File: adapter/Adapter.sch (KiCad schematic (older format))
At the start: 13 parts, among them J1 USB_B_Micro, J2 2040210-1, J3 USB_C_Receptacle, J4 Conn_01x01, J5 Conn_01x01

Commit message: Design considerations and fixed most external circuitry for STM32
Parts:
- removed J4, J5: Conn_01x01, TestPoint:TestPoint_Keystone_5015_Micro-Minature, symbol Connector_Generic:Conn_01x01
- removed JP1, JP2: Jumper, Jumper:SolderJumper-2_P1.3mm_Bridged_RoundedPad1.0x1.5mm, symbol Device:Jumper
- removed R1: 1k, Resistor_SMD:R_0805_2012Metric, symbol Device:R
- removed R2: 2k, Resistor_SMD:R_0805_2012Metric, symbol Device:R
- added C1, C2: C_Small, symbol Device:C_Small
- added C? (x2): 20p, symbol Device:C_Small
- added C? (x5): 100n, symbol Device:C_Small
- added C?: C, symbol Device:C
- added J?: Conn_01x05_Male, symbol Connector:Conn_01x05_Male
- added L1: Ferrite_Bead_Small, symbol Device:Ferrite_Bead_Small
- added L2: CIM05U601NC, symbol Device:Ferrite_Bead_Small
- added Q?: IRLML2244TRPBF, symbol Device:Q_PMOS_GSD
- added R?: 100k, symbol Device:R
- added U1: SN75DP119, SN75DP118:QFN-20-1EP_4x4mm_P0.5mm_EP2.5x2.5mm, symbol DisplayPort_Redriver:SN75DP119
- added U2: AZ1117-3.3, symbol Regulator_Linear:AZ1117-3.3
- added U3: STM32F072C8Tx, Package_QFP:LQFP-48_7x7mm_P0.5mm, symbol MCU_ST_STM32F0:STM32F072C8Tx
- added Y?: 8MHZ, symbol Device:Crystal
- J1: symbol Connector_Specialized:USB_B_Micro -> Connector:USB_B_Micro
- J2: footprint digikey-footprints:DisplayPort_2040210-1 -> DP1RD20JQ1R400:DP1RD20JQ1R400
- J3: footprint USB_C:DX07S024WJ3R400 -> Connector_USB:USB_C_Receptacle_Amphenol_12401548E4-2A_CircularHoles; symbol Connector_Specialized:USB_C_Receptacle -> Connector:USB_C_Receptacle
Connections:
- net labels added: +3V3, DP_IN_0+, DP_IN_0-, DP_IN_1+, DP_IN_1-, DP_IN_2+, DP_IN_2-, DP_IN_3+, DP_IN_3-, DP_OUT_0+, DP_OUT_0-, DP_OUT_1+, DP_OUT_1-, EN_CTL, EQ_CTL, EXT_3.3V, PRE_CTL, SWCLK, SWDIO, VBUS_EN, VOD_CTL, nRESET
- net labels removed: D2+, D2-, DP0+, DP0-, DP1+, DP1-, DP2+, DP2-, DP3+, DP3-, pAUX+, pAUX-
- wire segments 51 -> 125
- no-connect marks 0 -> 9
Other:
- note added: "BOM\n\n8MHz Crystal -> In Stock??"
- note added: "Design Considerations.\n\nWhat to do with extra lane on DP redriver?\n -> route DP1+- as well, disable lane through EN-Z in software\n\nTerminate extra DP lanes or leave open? \n\n\nMake use of USB in STM32?-> Break out to pin headers?\n-> maybe, just maybe: connect to device USB, and leave floating?\n\n\nConnect CONFIG1/CONFIG2 to microcontroller, just in case? -> Connect CONFIG2 to CEC AF-Pin\n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"
- note added: "KiCAD Questions?\n\nEasiest way to place test points?"
- note added: "STM32 Q&A:\nDoes the VBAT need to be connected?\nDo we need special decoupling for AVDD?\nWhich are the analog pins?\n\nHow to do reset? -> can it be left floating / on SWD connector?\n\n\nWhat is BOOT0?\n\n\nHow we do programming? -> expose SWD Pins + VDD + RESET\n\nDo PF0/1 have a special function? -> Yes, the Mhz Quartz\n\nOpt to not populate Crystal? F0x2 is "crystalless USB type""
- note added: "SWD Connector\nCheck congruence with nucleo board??"
- moved on the sheet: CC1, CC2, D2+1, D2-1, J2

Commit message: cleared a bunch of questions
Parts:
- added R2, R3: <5k?, symbol Device:R
- added R4, R6: 200, symbol Device:R
- added R5, R7: 100, symbol Device:R
- added R8, R9: NF, Resistor_SMD:R_0603_1608Metric_Pad1.05x0.95mm_HandSolder, symbol Device:R
- C1, C2: value C_Small -> 100n
- C3: renamed from C?; value C -> 4u7
- J2: Digi-Key_PN A99344-ND -> (none); MPN 2040210-1 -> DP1R020JQ3
- gave numbers to parts that had none: 11
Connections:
- net CC1: now also R2.2, R4.1, R5.2
- net CC2: now also R3.2, R6.1, R7.2
- net D+: now also R9.1
- net D-: now also R8.1
- net HPD: now also U3.30 (PA9)
- net VBUS_EN: now also U3.21 (PB10)
- net at U3.32 (PA11): now also R8.2
- net at U3.33 (PA12): now also R9.2
- net at C9.1, Y1.1: no longer U3.5 (PF0)
- net at C10.1, Y1.2: no longer U3.6 (PF1)
- new net CC1_EN: R2.1
- new net CC1_RX: R4.2
- new net CC1_TX: R5.1
- new net CC2_EN: R3.1
- new net CC2_RX: R6.2
- new net CC2_TX: R7.1
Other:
- note added: "Design Considerations.\n\nWhat to do with extra lane on DP redriver?\n -> route DP1+- as well, disable lane through EN-Z in software\n-> dont route, save hassle, focus on matching DP0\n\nTerminate extra DP lanes or leave open? \n\n\nMake use of USB in STM32?-> Break out to pin headers?\n-> maybe, just maybe: connect to device USB, and leave floating?\n\n\nConnect CONFIG1/CONFIG2 to microcontrolle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"
- note added: "STM32 Q&A:\nDoes the VBAT need to be connected?\nDo we need special decoupling for AVDD?\n\nWhich are the analog pins?\nstm32f072rb.pdf p.33 ff -> PA0-PA7, PB0-\n\n5V Tolerant pins?\n-> PF0-1, PB10-11\n\n\nHow to do reset? -> can it be left floating / on SWD connector?\n\n\nWhat is BOOT0?\n\n\nHow we do programming? -> expose SWD Pins + VDD + RESET\n\nDo PF0/1 have a special function? -> Yes, the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"
- note added: "SWD Connector\nCheck congruence with nucleo board??\nSTMboards have 6 pins??"
- note removed: "BOM\n\n8MHz Crystal -> In Stock??"
- note removed: "Design Considerations.\n\nWhat to do with extra lane on DP redriver?\n -> route DP1+- as well, disable lane through EN-Z in software\n\nTerminate extra DP lanes or leave open? \n\n\nMake use of USB in STM32?-> Break out to pin headers?\n-> maybe, just maybe: connect to device USB, and leave floating?\n\n\nConnect CONFIG1/CONFIG2 to microcontroller, just in case? -> Connect CONFIG2 to CEC AF-Pin\n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"
- note removed: "STM32 Q&A:\nDoes the VBAT need to be connected?\nDo we need special decoupling for AVDD?\nWhich are the analog pins?\n\nHow to do reset? -> can it be left floating / on SWD connector?\n\n\nWhat is BOOT0?\n\n\nHow we do programming? -> expose SWD Pins + VDD + RESET\n\nDo PF0/1 have a special function? -> Yes, the Mhz Quartz\n\nOpt to not populate Crystal? F0x2 is "crystalless USB type""
- note removed: "SWD Connector\nCheck congruence with nucleo board??"
- moved on the sheet: C10, C9, Y1

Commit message: used most of stm32 pinning from twinkie board
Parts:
- added C?: 4u7, symbol Device:C_Small
- added C?: 1u, symbol Device:C_Small
- added D?: LED_ARGB, symbol Device:LED_ARGB
- added R? (x3): R, symbol Device:R
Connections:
- net labels added: LED_B_L, LED_G_L, LED_R_L, TX_CLK
- wire segments 141 -> 175
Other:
- moved on the sheet: C10, C5, C6, C7, C8, C9, L2, Y1

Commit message: pre-place most of components
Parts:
- added C13, C14, C15: 100n, Capacitor_SMD:C_0402_1005Metric, symbol Device:C_Small
- added C20: 4u7, Capacitor_SMD:C_0603_1608Metric_Pad1.05x0.95mm_HandSolder, symbol Device:C
- added R13, R14, R15: R, Resistor_SMD:R_0603_1608Metric_Pad1.05x0.95mm_HandSolder, symbol Device:R
- added SW1: SW_Push, symbol Switch:SW_Push
- C1, C10, C3, C4, C5, C6, C7, C8, C9: footprint (none) -> Capacitor_SMD:C_0603_1608Metric_Pad1.05x0.95mm_HandSolder
- C11, C12: renamed from C?; footprint (none) -> Capacitor_SMD:C_0603_1608Metric_Pad1.05x0.95mm_HandSolder
- C2: footprint (none) -> Capacitor_SMD:C_0402_1005Metric
- D1: renamed from D?; footprint (none) -> LED_SMD:LED_Cree-PLCC4_3.2x2.8mm_CCW; symbol Device:LED_ARGB -> Device:LED_RAGB; MFP (none) -> CLVBA-FKA-CAEDH8BBB7a363
- J4: footprint (none) -> Connector_PinHeader_2.54mm:PinHeader_1x05_P2.54mm_Vertical
- L1: value Ferrite_Bead_Small -> CIM05U601NC; footprint (none) -> Inductor_SMD:L_0603_1608Metric_Pad1.05x0.95mm_HandSolder
- L2: footprint (none) -> Inductor_SMD:L_0603_1608Metric_Pad1.05x0.95mm_HandSolder
- Q1: footprint (none) -> Package_TO_SOT_SMD:SOT-23
- R1, R2, R3, R4, R5, R6, R7: footprint (none) -> Resistor_SMD:R_0603_1608Metric_Pad1.05x0.95mm_HandSolder
- R10, R11, R12: renamed from R?; footprint (none) -> Resistor_SMD:R_0603_1608Metric_Pad1.05x0.95mm_HandSolder
- U1: MFP (none) -> SN75DP119RGYR
- U2: footprint (none) -> Package_TO_SOT_SMD:SOT-223; MFP (none) -> AZ1117IH-3.3TRG1
- Y1: footprint (none) -> Crystal:Crystal_SMD_TXC_7A-2Pin_5x3.2mm; MFP (none) -> 7A-8.000MAAE-T
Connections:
- net labels added: BOOT, UART_RX, UART_TX, VDD, VDDA
- wire segments 175 -> 199
- no-connect marks 9 -> 13
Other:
- note added: "AC coupling on RX side?\n\nWhich type of couple cap?"
- note added: "STM32 Q&A:\nDoes the VBAT need to be connected? yes, to VDD\nDo we need special decoupling for AVDD? yes, with bead\n\nWhich are the analog pins?\nstm32f072rb.pdf p.33 ff -> PA0-PA7, PB0-1\n\n\n5V Tolerant pins?\n-> PF0-1, PB10-11\n\n\nHow to do reset? -> can it be left floating / on SWD connector?\n\n\nWhat is BOOT0?\n\n\nHow we do programming? -> expose SWD Pins + VDD + RESET\n\nDo PF0/1 have a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"
- note removed: "KiCAD Questions?\n\nEasiest way to place test points?"
- note removed: "STM32 Q&A:\nDoes the VBAT need to be connected?\nDo we need special decoupling for AVDD?\n\nWhich are the analog pins?\nstm32f072rb.pdf p.33 ff -> PA0-PA7, PB0-\n\n5V Tolerant pins?\n-> PF0-1, PB10-11\n\n\nHow to do reset? -> can it be left floating / on SWD connector?\n\n\nWhat is BOOT0?\n\n\nHow we do programming? -> expose SWD Pins + VDD + RESET\n\nDo PF0/1 have a special function? -> Yes, the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"
- moved on the sheet: C10, C11, C12, C2, C4, C5, C6, C7, C8, C9, J4, L2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

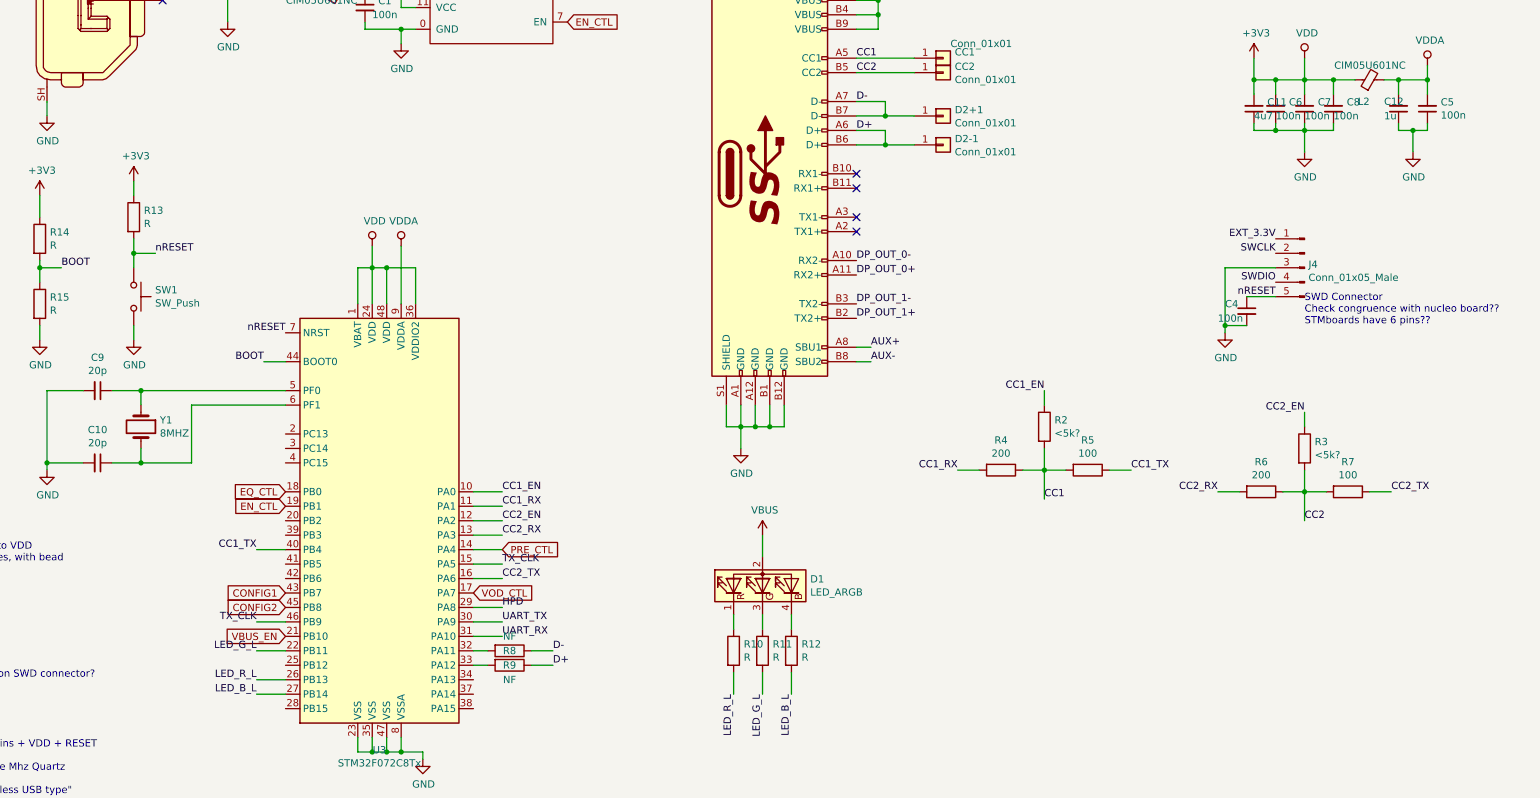
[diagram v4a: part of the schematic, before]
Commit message: Added 3D STEP for micro-USB Jack
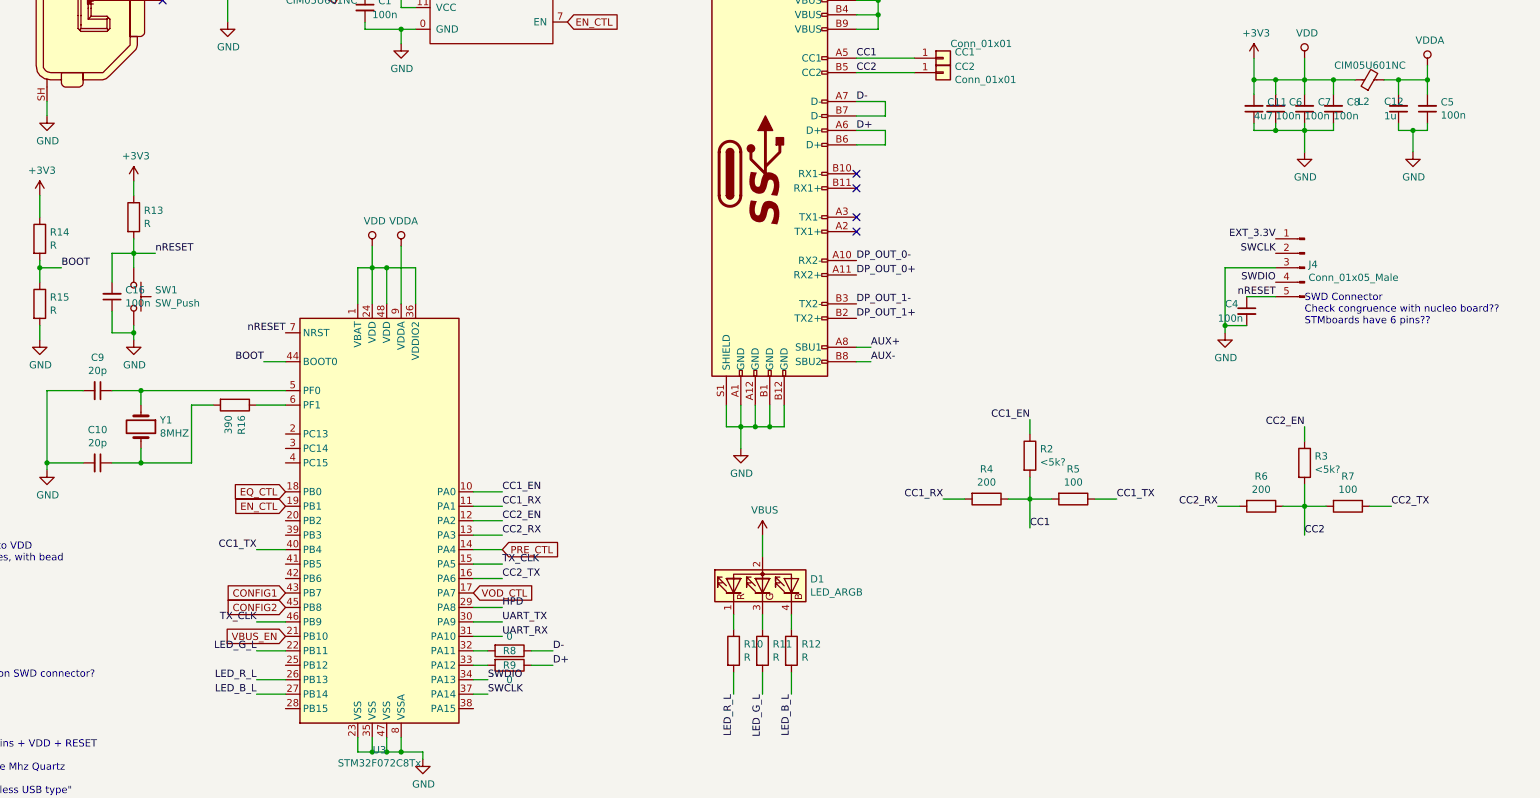
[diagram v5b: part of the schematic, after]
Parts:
- removed D2+1, D2-1: Conn_01x01, TestPoint:TestPoint_Pad_1.0x1.0mm, symbol Connector_Generic:Conn_01x01
- added C16: 100n, Capacitor_SMD:C_0603_1608Metric_Pad1.05x0.95mm_HandSolder, symbol Device:C_Small
- added R16: 390, Resistor_SMD:R_0603_1608Metric_Pad1.05x0.95mm_HandSolder, symbol Device:R
- C10, C9: MFP (none) -> CC0603JRNPO9BN120
- C20, C3: MFP (none) -> JMK107BJ475KA-T
- J1: MFP (none) -> 10118194-0001LF
- J2: MFP (none) -> DP1R020JQ3; MPN DP1R020JQ3 -> (none)
- J3: MFP (none) -> DX07S024XJ4R250
- Q1: MFP (none) -> IRLML2244TRPBF
- R8, R9: value NF -> 0
- SW1: footprint (none) -> Button_Switch_SMD:SW_SPST_PTS645; MFP (none) -> PTS647SN38SMTR2LFS
- U3: MFP (none) -> STM32F072CBT6
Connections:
- net GND: now also C16.1
- net SWCLK: now also U3.37 (PA14)
- net SWDIO: now also U3.34 (PA13)
- net nRESET: now also C16.2
- net at C10.1, Y1.2: now also R16.2; no longer U3.6 (PF1)
- new net: R16.1, U3.6 (PF1)
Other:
- moved on the sheet: R2, R3, R4, R5, R6, R7

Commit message: Step file for MicroUSB
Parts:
- added R17: 0, Resistor_SMD:R_0603_1608Metric_Pad1.05x0.95mm_HandSolder, symbol Device:R
- added SW2: SW_Push, Button_Switch_SMD:SW_SPST_PTS645, symbol Switch:SW_Push
- J1: footprint digikey-footprints:USB_Micro_B_Female_10118194-0001LF -> USB_MicroB:CONN-10118194-0001LF-FCI
- J2: MFP DP1R020JQ3 -> DP1RD20JQ1R400; Notes (none) -> Compatible Molex 47272-0001
- J3: footprint Connector_USB:USB_C_Receptacle_Amphenol_12401548E4-2A_CircularHoles -> Connector_USB:USB_C_Receptacle_Amphenol_12401610E4-2A; MFP DX07S024XJ4R250 -> 12401598E4#2A
- R13, R15: value R -> 100k; MFP (none) -> RC0603FR-13100KL
- R14: value R -> 0
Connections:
- net +3V3: now also SW2.1; no longer R14.1
- net AUX+: now also R17.1
- net AUX-: now also R14.1
- net BOOT: now also SW2.2; no longer R14.2
- net CC1_EN: now also U3.41 (PB5); no longer U3.10 (PA0)
- net CC2_EN: now also U3.42 (PB6); no longer U3.12 (PA2)
- net CONFIG1: no longer U3.43 (PB7)
- net CONFIG2: no longer U3.45 (PB8)
- net EN_CTL: now also U3.10 (PA0); no longer U3.19 (PB1)
- net PRE_CTL: now also U3.12 (PA2); no longer U3.14 (PA4)
- net TX_CLK: now also U3.19 (PB1), U3.39 (PB3); no longer U3.15 (PA5), U3.46 (PB9)
- new net: R14.2, U3.14 (PA4)
- new net: R17.2, U3.15 (PA5)
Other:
- moved on the sheet: C1, C10, C11, C12, C13, C14, C15, C16, C2, C20, C3, C4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

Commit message: sync changs from tmp checkout
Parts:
- J1: symbol Connector:USB_B_Micro -> Digikey_USB-DVI-HDMI:10118194-0001LF
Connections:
- net GND: now also J1.SH; no longer J1.6 (Shield)
- net DP_OUT_1+: no longer names the net of J3.B2 (TX2+)
- net DP_OUT_1-: no longer names the net of J3.B3 (TX2-)
- no-connect marks 13 -> 16
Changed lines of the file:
@@
 $EndComp
 $Comp
-L Connector:USB_B_Micro J1
+L Digikey_USB-DVI-HDMI:10118194-0001LF J1
 U 1 1 5B41DD1F
 P 2650 1350
@@
 Text Label 3000 1350 0    50   ~ 0
 D+
-Text Label 3000 1450 0    50   ~ 0
+Text Label 3000 1250 0    50   ~ 0
 D-
 $Comp
 L power:GND #PWR0101
 U 1 1 5B41DEE2
-P 2650 1900
-F 0 "#PWR0101" H 2650 1650 50  0001 C CNN
-F 1 "GND" H 2655 1727 50  0000 C CNN
-F 2 "" H 2650 1900 50  0001 C CNN
-F 3 "" H 2650 1900 50  0001 C CNN
-	1    2650 1900
-	1    0    0    -1
-$EndComp
-Wire Wire Line
-	2650 1900 2650 1800
+P 3000 2250
+F 0 "#PWR0101" H 3000 2000 50  0001 C CNN
+F 1 "GND" H 3005 2077 50  0000 C CNN
+F 2 "" H 3000 2250 50  0001 C CNN
+F 3 "" H 3000 2250 50  0001 C CNN
+	1    3000 2250
+	1    0    0    -1
+$EndComp
+Wire Wire Line
+	3000 2250 3000 2150
 $Comp
 L power:VBUS #PWR0102
@@
 Text Label 9850 3700 0    50   ~ 0
 DP_OUT_0-
-Text Label 9850 4000 0    50   ~ 0
-DP_OUT_1-
-Text Label 9850 4100 0    50   ~ 0
-DP_OUT_1+
 Text Label 5000 2000 0    50   ~ 0
 DP_IN_0+
@@
 	3000 1350 2950 1350
 Wire Wire Line
-	3000 1450 2950 1450
+	3000 1250 2950 1250
 $Comp
 L Connector_Generic:Conn_01x01 CC2
@@
 Wire Wire Line
 	10050 2800 10050 2900
-Wire Wire Line
-	2550 1750 2550 1800
-Wire Wire Line
-	2550 1800 2650 1800
-Connection ~ 2650 1800
-Wire Wire Line
-	2650 1800 2650 1750
+Connection ~ 3000 2150
 $Comp
 L MCU_ST_STM32F0:STM32F072C8Tx U3
@@
 Wire Wire Line
 	4950 6500 4950 6600
+NoConn ~ 9850 4000
+NoConn ~ 9850 4100
+NoConn ~ 2950 1450
+Wire Wire Line
+	3000 1550 2950 1550
+Wire Wire Line
+	3000 1550 3000 2150
+Wire Wire Line
+	2550 2150 2550 1950
+Wire Wire Line
+	2550 2150 3000 2150
 $EndSCHEMATC

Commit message: renamed custom footprints
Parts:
- J2: footprint DP1RD20JQ1R400:DP1RD20JQ1R400 -> Displayport:DP1RD20JQ1R400
- U1: footprint SN75DP118:QFN-20-1EP_4x4mm_P0.5mm_EP2.5x2.5mm -> SN75DP119:QFN-20-1EP_4x4mm_P0.5mm_EP2.5x2.5mm
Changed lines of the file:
@@
 F 0 "J2" H 4500 2737 60  0000 C CNN
 F 1 "2040210-1" H 4500 2631 60  0000 C CNN
-F 2 "DP1RD20JQ1R400:DP1RD20JQ1R400" H 4700 2000 60  0001 L CNN
+F 2 "Displayport:DP1RD20JQ1R400" H 4700 2000 60  0001 L CNN
 F 3 "http://www.te.com/commerce/DocumentDelivery/DDEController?Action=srchrtrv&DocNm=2040210&DocType=Customer+Drawing&DocLang=Japanese" H 4700 2100 60  0001 L CNN
 F 4 "CONN RCPT DISPLAYPRT 1.1A 20POS" H 4700 2800 60  0001 L CNN "Description"
@@
 F 0 "U1" H 7175 3015 50  0000 C CNN
 F 1 "SN75DP119" H 7175 2924 50  0000 C CNN
-F 2 "SN75DP118:QFN-20-1EP_4x4mm_P0.5mm_EP2.5x2.5mm" H 7200 2000 50  0001 C CNN
+F 2 "SN75DP119:QFN-20-1EP_4x4mm_P0.5mm_EP2.5x2.5mm" H 7200 2000 50  0001 C CNN
 F 3 "" H 7200 2000 50  0001 C CNN
 F 4 "SN75DP119RGYR" H 7150 2150 50  0001 C CNN "MFP"
